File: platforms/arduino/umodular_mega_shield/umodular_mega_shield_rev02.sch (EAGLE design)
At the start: 29 parts, among them IC1 23LC1024, IC2 74HC4050/CD4050, IC3 6N138, U1 ARDUINO-MEGA-SHIELD

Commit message: added platform arduino mega shiled a external power connector.
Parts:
- added POWER: +5V, SparkFun-Connectors:CONN_02LOCK_LONGPADS
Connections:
- net GND: now also POWER.2
- net VCC: now also POWER.1
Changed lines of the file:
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@@
 <part name="C2" library="rcl" deviceset="C-US" device="050-024X044" value="100nf"/>
 <part name="R9" library="rcl" deviceset="R-US_" device="0204/7" value="2.2k"/>
+<part name="POWER" library="SparkFun-Connectors" deviceset="CONN_02" device="LOCK_LONGPADS" value="+5V"/>
 </parts>
 <sheets>
@@
 <instance part="ANALOG5" gate="G$1" x="325.12" y="127.635"/>
 <instance part="ANALOG6" gate="G$1" x="325.12" y="97.155"/>
-<instance part="FRAME1" gate="G$1" x="0" y="0"/>
+<instance part="FRAME1" gate="G$1" x="0" y="0" smashed="yes">
+<attribute name="DRAWING_NAME" x="319.151" y="19.431" size="2.54" layer="94" font="vector"/>
+<attribute name="LAST_DATE_TIME" x="309.753" y="9.525" size="2.286" layer="94" font="vector"/>
+<attribute name="SHEET" x="368.3" y="4.445" size="2.54" layer="94" font="vector"/>
+</instance>
 <instance part="U1" gate="G$1" x="177.8" y="146.05"/>
 <instance part="SPI3" gate="G$1" x="44.45" y="45.72"/>
@@
 <instance part="C2" gate="G$1" x="99.06" y="38.1"/>
 <instance part="R9" gate="G$1" x="27.94" y="144.78"/>
+<instance part="POWER" gate="G$1" x="226.06" y="231.14"/>
 </instances>
 <busses>
@@
 <wire x1="38.1" y1="200.66" x2="22.86" y2="200.66" width="0.1524" layer="91"/>
 <label x="12.7" y="200.66" size="1.778" layer="95"/>
+</segment>
+<segment>
+<pinref part="POWER" gate="G$1" pin="2"/>
+<wire x1="233.68" y1="233.68" x2="248.92" y2="233.68" width="0.1524" layer="91"/>
+<label x="248.92" y="233.68" size="1.778" layer="95"/>
 </segment>
 </net>
@@
 <label x="68.58" y="119.38" size="1.778" layer="95"/>
 </segment>
+<segment>
+<pinref part="POWER" gate="G$1" pin="1"/>
+<wire x1="233.68" y1="231.14" x2="248.92" y2="231.14" width="0.1524" layer="91"/>
+<label x="248.92" y="231.14" size="1.778" layer="95"/>
+</segment>
 </net>

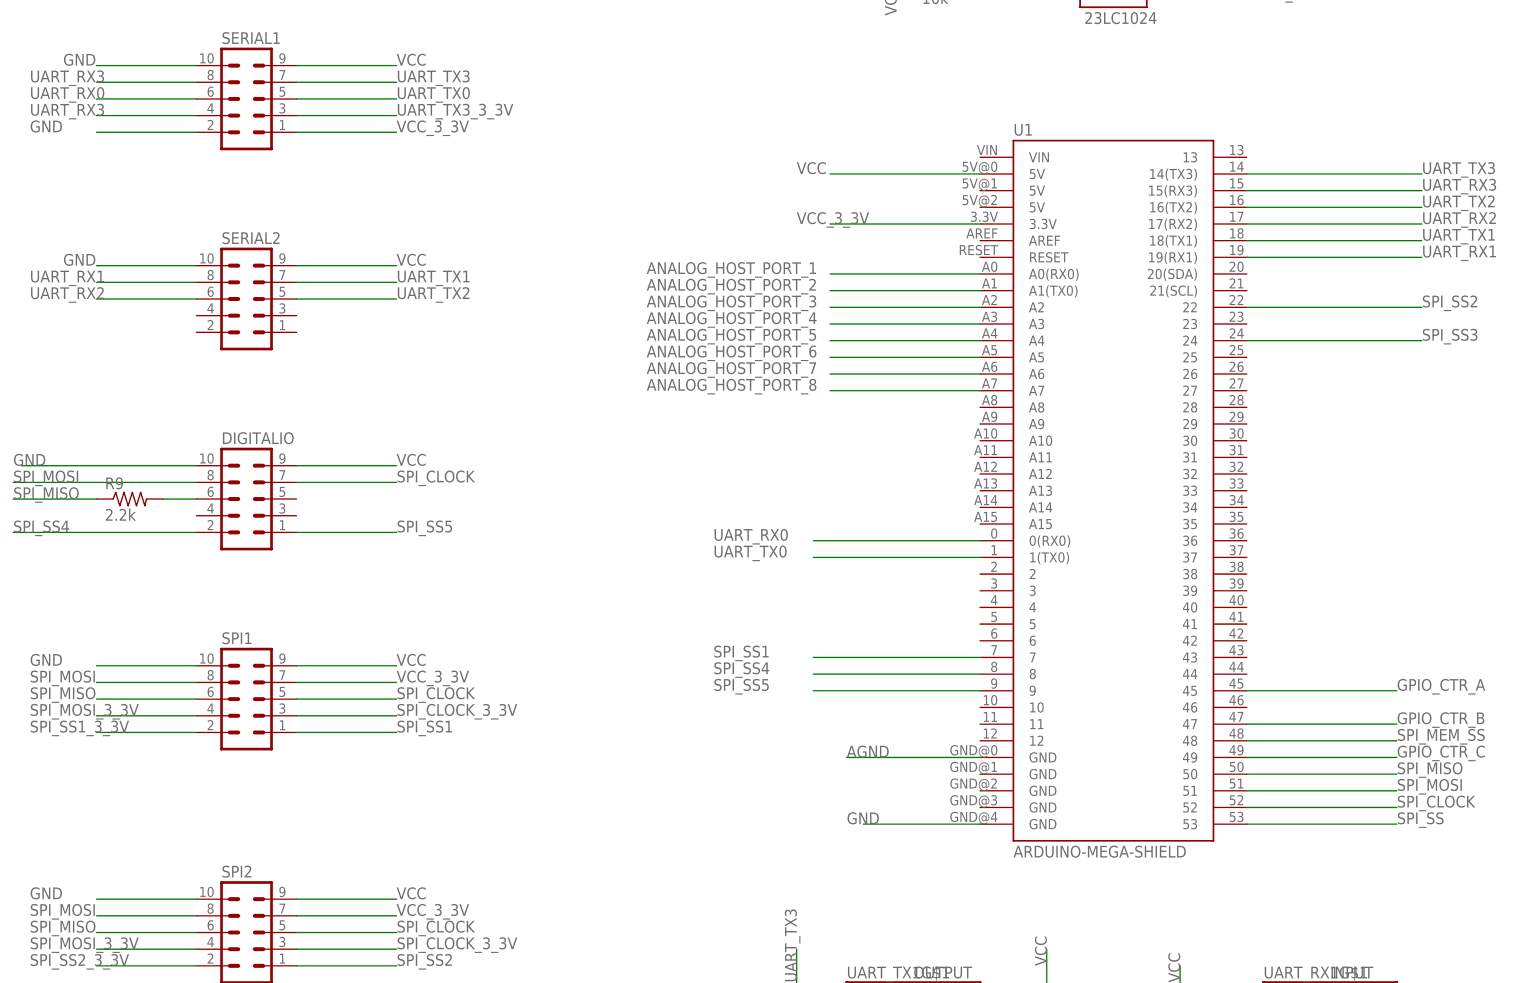
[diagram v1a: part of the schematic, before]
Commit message: Change shift registers from SPI hardware based to Software implementation. Free the SPI bus for things more important(SDCARD and RAM)
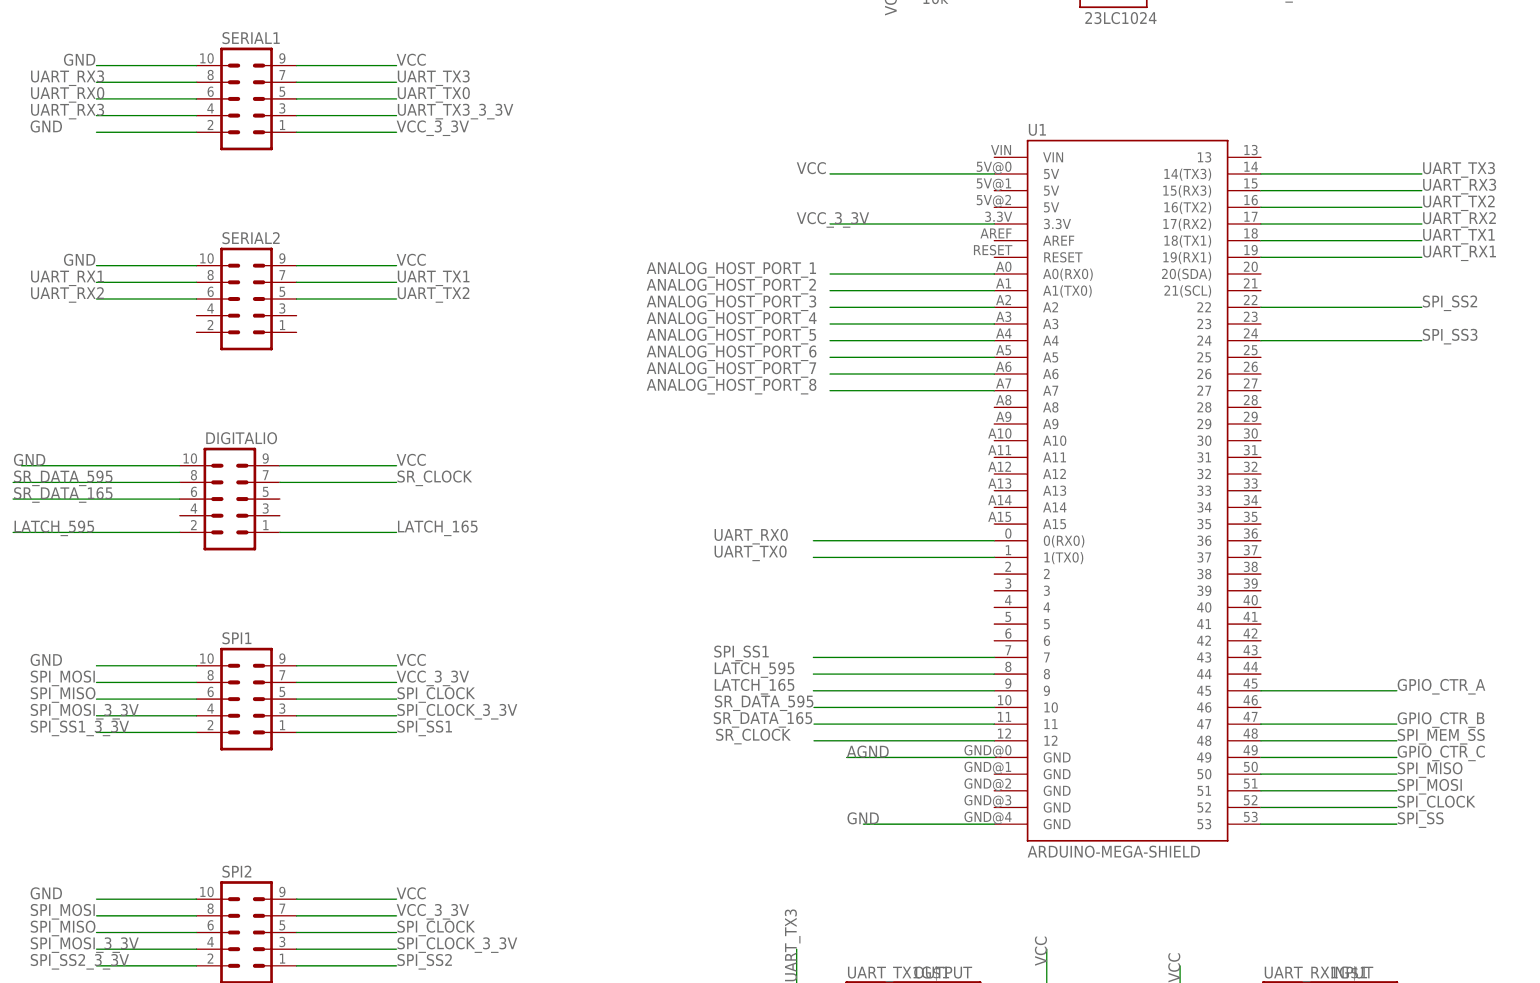
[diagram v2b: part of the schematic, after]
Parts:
- removed R9: 2.2k, rcl:R-US_0204/7
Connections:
- net SPI_SS4 renamed LATCH_595
- net SPI_SS5 renamed LATCH_165
- removed net N$9: DIGITALIO.6, R9.2
- new net SR_CLOCK: DIGITALIO.7, U1.12
- new net SR_DATA_165: DIGITALIO.6, U1.11
- new net SR_DATA_595: DIGITALIO.8, U1.10
- net SPI_CLOCK: no longer DIGITALIO.7
- net SPI_MISO: no longer R9.1
- net SPI_MOSI: no longer DIGITALIO.8
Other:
- moved on the sheet: DIGITALIO, U1

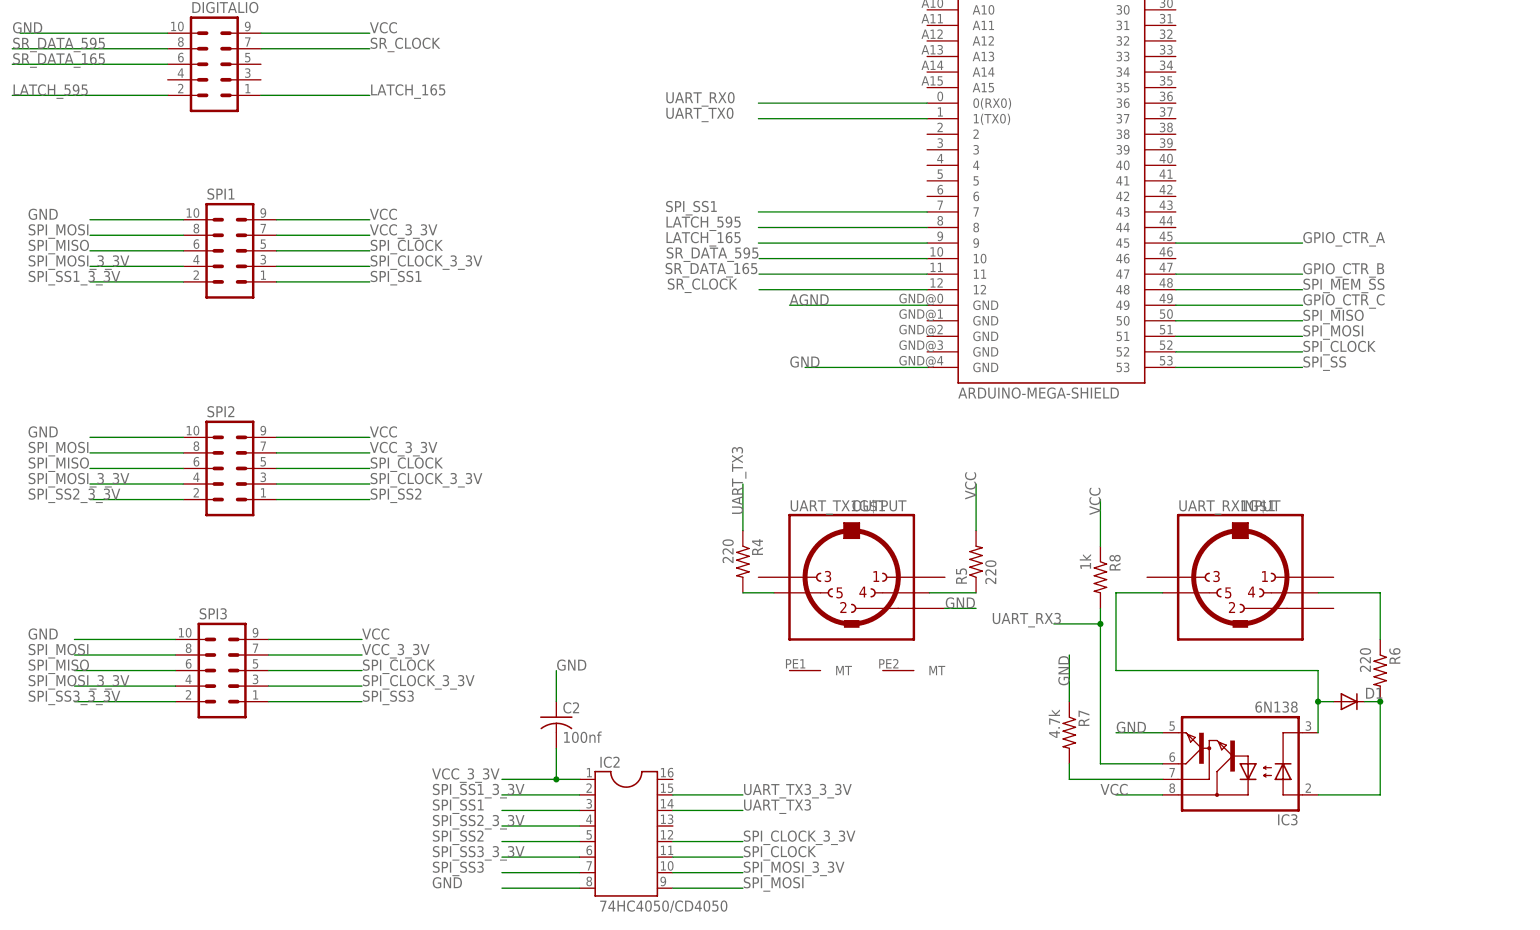
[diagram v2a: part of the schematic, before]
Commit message: changes that reflects main hardware connections of project. Hardware SPI are only for RAM memory, sdcard goes via SoftSPI(exclusive wire path) and shift registers 165 and 595 goes via shiftIn and shiftOut
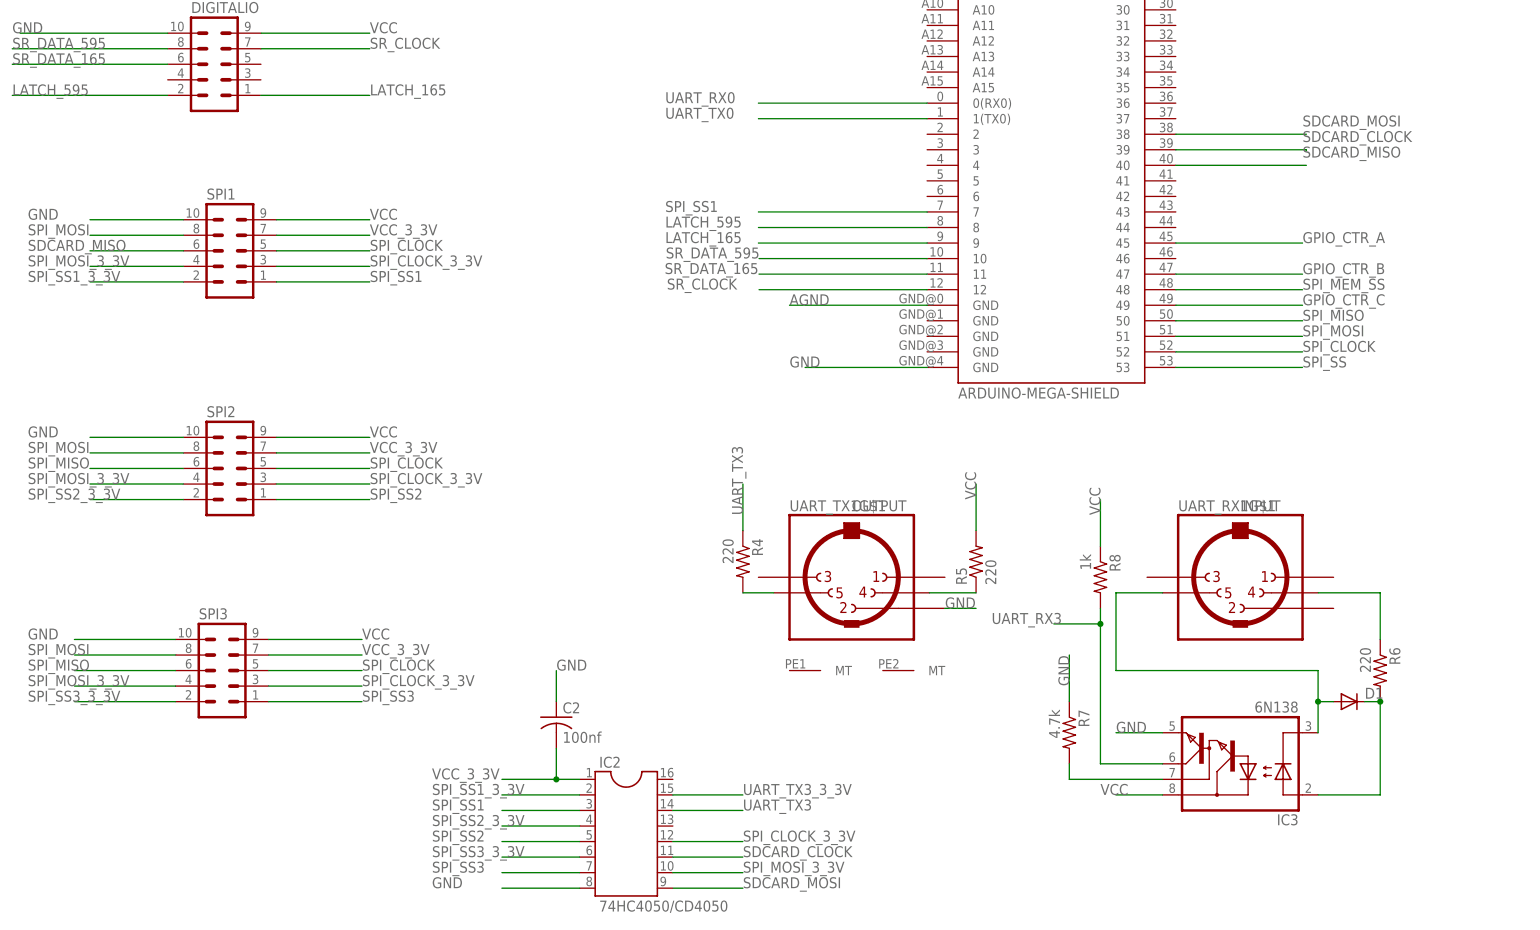
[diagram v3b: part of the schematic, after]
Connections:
- new net SDCARD_CLOCK: IC2.11, U1.39
- new net SDCARD_MISO: SPI1.6, U1.40
- new net SDCARD_MOSI: IC2.9, U1.38
- net SPI_CLOCK: no longer IC2.11
- net SPI_MISO: no longer SPI1.6
- net SPI_MOSI: no longer IC2.9
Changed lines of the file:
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@@
 <setting verticaltext="up"/>
 </settings>
-<grid distance="0.001" unitdist="inch" unit="inch" style="lines" multiple="1" display="no" altdistance="0.01" altunitdist="inch" altunit="inch"/>
+<grid distance="0.1" unitdist="inch" unit="inch" style="lines" multiple="1" display="no" altdistance="0.01" altunitdist="inch" altunit="inch"/>
 <layers>
 <layer number="1" name="Top" color="4" fill="1" visible="no" active="no"/>
@@
 <wire x1="53.34" y1="114.3" x2="68.58" y2="114.3" width="0.1524" layer="91"/>
 </segment>
-<segment>
-<pinref part="IC2" gate="G$1" pin="11"/>
-<wire x1="118.11" y1="15.24" x2="129.54" y2="15.24" width="0.1524" layer="91"/>
-<label x="129.54" y="15.24" size="1.778" layer="95"/>
-</segment>
 </net>
 <net name="SPI_MISO" class="0">
-<segment>
-<pinref part="SPI1" gate="G$1" pin="6"/>
-<wire x1="38.1" y1="114.3" x2="22.86" y2="114.3" width="0.1524" layer="91"/>
-<label x="12.7" y="114.3" size="1.778" layer="95"/>
-</segment>
 <segment>
 <pinref part="U1" gate="G$1" pin="50"/>
@@
 <pinref part="SPI3" gate="G$1" pin="8"/>
 <label x="12.7" y="48.26" size="1.778" layer="95"/>
-</segment>
-<segment>
-<pinref part="IC2" gate="G$1" pin="9"/>
-<wire x1="118.11" y1="10.16" x2="129.54" y2="10.16" width="0.1524" layer="91"/>
-<label x="129.54" y="10.16" size="1.778" layer="95"/>
 </segment>
 </net>
@@
 </segment>
 </net>
+<net name="SDCARD_MOSI" class="0">
+<segment>
+<pinref part="U1" gate="G$1" pin="38"/>
+<wire x1="200.279" y1="133.35" x2="221.615" y2="133.35" width="0.1524" layer="91"/>
+<label x="220.98" y="134.62" size="1.778" layer="95"/>
+</segment>
+<segment>
+<pinref part="IC2" gate="G$1" pin="9"/>
+<wire x1="118.11" y1="10.16" x2="129.54" y2="10.16" width="0.1524" layer="91"/>
+<label x="129.54" y="10.16" size="1.778" layer="95"/>
+</segment>
+</net>
+<net name="SDCARD_CLOCK" class="0">
+<segment>
+<wire x1="200.279" y1="130.81" x2="221.615" y2="130.81" width="0.1524" layer="91"/>
+<wire x1="221.615" y1="130.81" x2="221.615" y2="130.683" width="0.1524" layer="91"/>
+<pinref part="U1" gate="G$1" pin="39"/>
+<label x="220.98" y="132.08" size="1.778" layer="95"/>
+</segment>
+<segment>
+<pinref part="IC2" gate="G$1" pin="11"/>
+<wire x1="118.11" y1="15.24" x2="129.54" y2="15.24" width="0.1524" layer="91"/>
+<label x="129.54" y="15.24" size="1.778" layer="95"/>
+</segment>
+</net>
+<net name="SDCARD_MISO" class="0">
+<segment>
+<pinref part="U1" gate="G$1" pin="40"/>
+<wire x1="200.279" y1="128.27" x2="221.615" y2="128.27" width="0.1524" layer="91"/>
+<label x="220.98" y="129.54" size="1.778" layer="95"/>
+</segment>
+<segment>
+<pinref part="SPI1" gate="G$1" pin="6"/>
+<wire x1="38.1" y1="114.3" x2="22.86" y2="114.3" width="0.1524" layer="91"/>
+<label x="12.7" y="114.3" size="1.778" layer="95"/>
+</segment>
+</net>
